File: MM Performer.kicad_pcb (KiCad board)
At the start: 4 copper layers, 75.2 x 85.7 mm, 44 parts, among them IC1 68000D, J1 VCC, J2 GND, J3 FPU Clock, U1 MC68030RC, U2 MC68881FN-SOC, U3 ATF16V8BJ, U4 ATF16V8BJ, U5 ATF16V8BJ, U6 ATF16V8BJ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

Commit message: Further signal tweaks
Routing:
- net /CLK_30: track 115.9 -> 127.8 mm
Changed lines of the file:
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@@
+	)
+	(segment
+		(start 75.507 129.725)
+		(end 75.057 130.175)
+		(width 0.4)
+		(layer "F.Cu")
+		(net 82)
 	)
 	(segment
@@
 	(segment
 		(start 70.231 130.175)
-		(end 106.68 130.175)
+		(end 75.057 130.175)
+		(width 0.4)
+		(layer "F.Cu")
+		(net 82)
+	)
+	(segment
+		(start 75.507 119.819)
+		(end 75.507 129.725)
 		(width 0.4)
 		(layer "F.Cu")
@@
 		(width 0.4)
 		(layer "F.Cu")
+		(net 82)
+	)
+	(segment
+		(start 76.454 118.872)
+		(end 75.507 119.819)
+		(width 0.4)
+		(layer "F.Cu")
+		(net 82)
+	)
+	(segment
+		(start 75.057 130.175)
+		(end 106.68 130.175)
+		(width 0.4)
+		(layer "F.Cu")

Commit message: Further tweaks
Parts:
- moved J2 8.93 mm to (106.8, 124.3)
- moved J1 8.39 mm to (97.5, 133.9)
- moved C1 7.89 mm to (105.4, 132.1), turned to 45 degrees
- moved J3 7.73 mm to (107.8, 86.2), turned to 180 degrees
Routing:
- net /CLK_30: track 127.8 -> 117.1 mm
- net /FPUCLK: track 39.5 -> 44.9 mm
- net GND: track 728.1 -> 723.6 mm
- net VCC: track 818.1 -> 814.0 mm

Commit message: Tweak placement again
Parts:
- C10: moved to B.Cu
- moved C10 2.79 mm to (69.1, 131.3)
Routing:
- net GND: track 723.6 -> 666.0 mm
- net VCC: track 814.0 -> 758.5 mm
- net /CLK_30: track 117.1 -> 121.9 mm, vias 1 -> 2
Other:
- board size 75.2 x 85.7 mm -> 75.6 x 87.1 mm

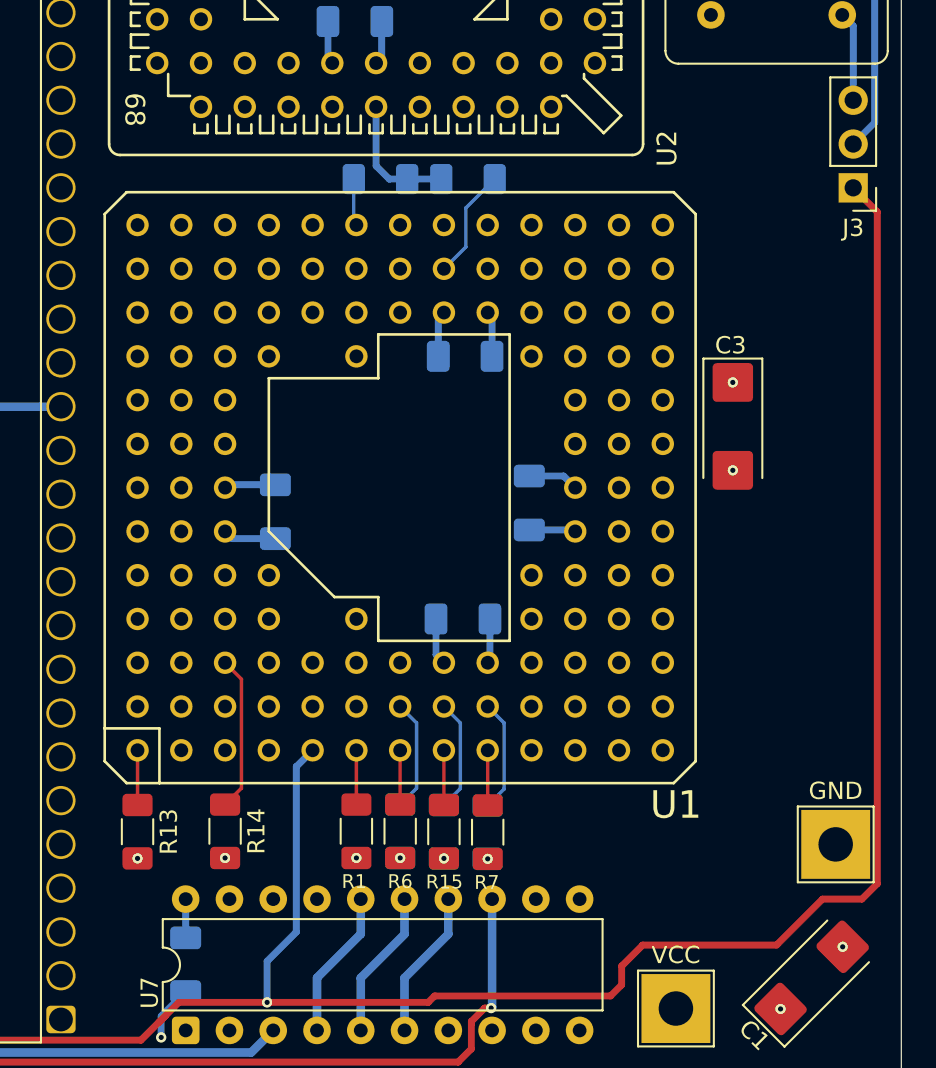
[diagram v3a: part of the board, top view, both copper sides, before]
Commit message: Reposition CPU
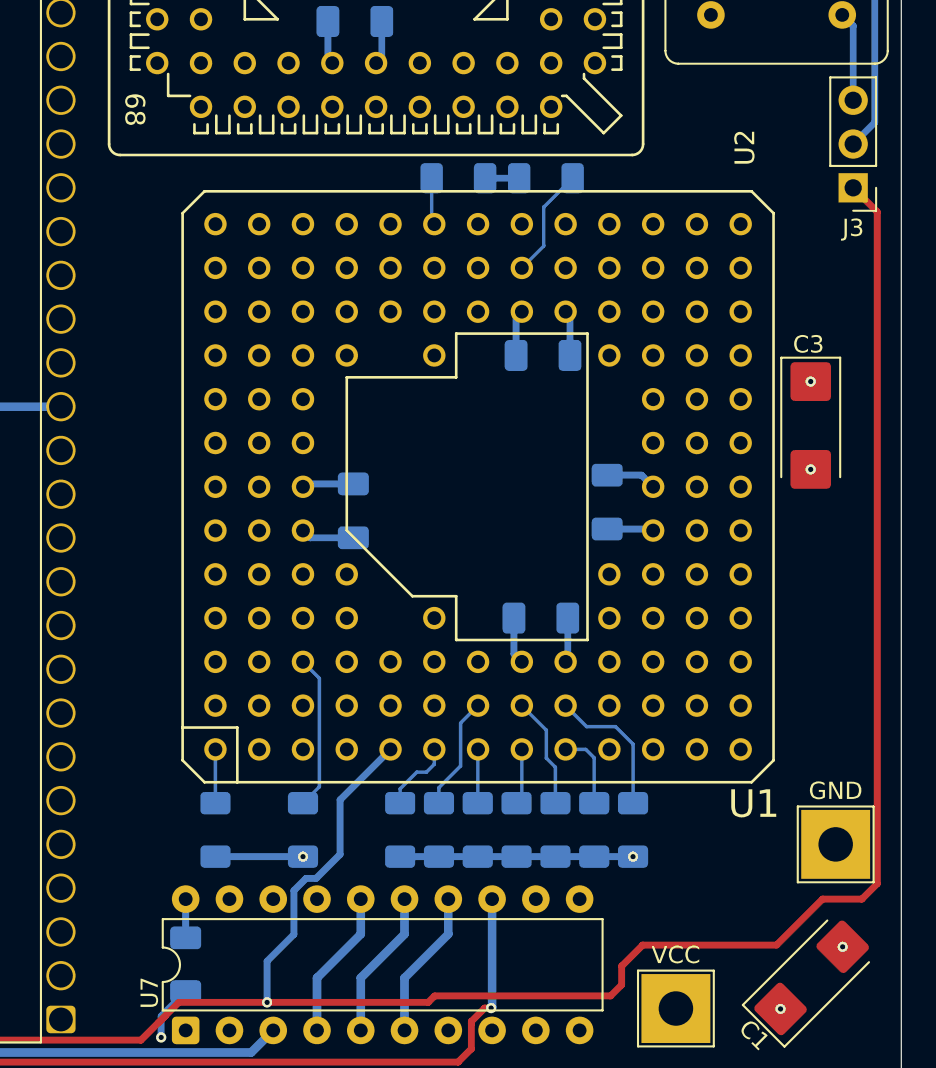
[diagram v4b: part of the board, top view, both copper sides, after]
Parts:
- R1, R13, R14, R15, R6, R7: moved to B.Cu
- moved R5 8.43 mm to (95.0, 123.5)
- moved R8 6.47 mm to (90.5, 123.5)
- moved R7 6.18 mm to (92.8, 123.5)
- moved R13 4.52 mm to (70.8, 123.5)
- moved R14 4.52 mm to (75.9, 123.5)
- moved C12 4.52 mm to (89.8, 96.0)
- moved C13 4.52 mm to (89.7, 111.2)
- moved C3 4.52 mm to (105.4, 100.0)
- moved C11 4.52 mm to (93.5, 104.5)
- moved C6 4.52 mm to (78.8, 105.0)
- moved R11 4.52 mm to (90.0, 85.7)
- moved R12 4.52 mm to (84.9, 85.7)
- moved U1 4.52 mm to (86.1, 103.6)
- moved R6 4.50 mm to (86.0, 123.5)
- moved R15 4.22 mm to (88.3, 123.5)
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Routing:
- net VCC: track 758.5 -> 749.0 mm, vias 17 -> 13
- net /CLK_30: track 121.9 -> 124.1 mm
- net //AS_30: track 6.53 -> 8.27 mm
- net //CBACK: track 3.20 -> 4.49 mm
- net //DSACK0: track 3.15 -> 4.27 mm

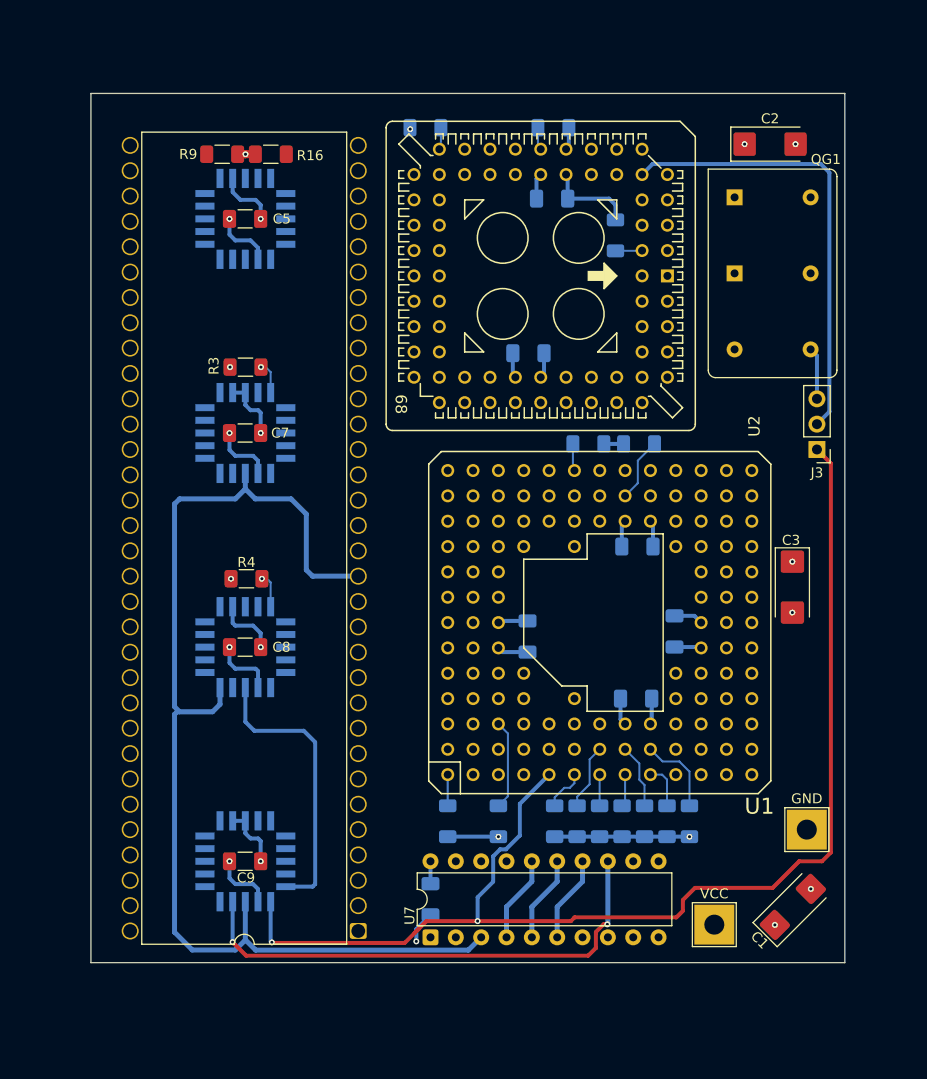
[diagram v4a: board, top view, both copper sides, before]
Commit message: Route traces, add zones
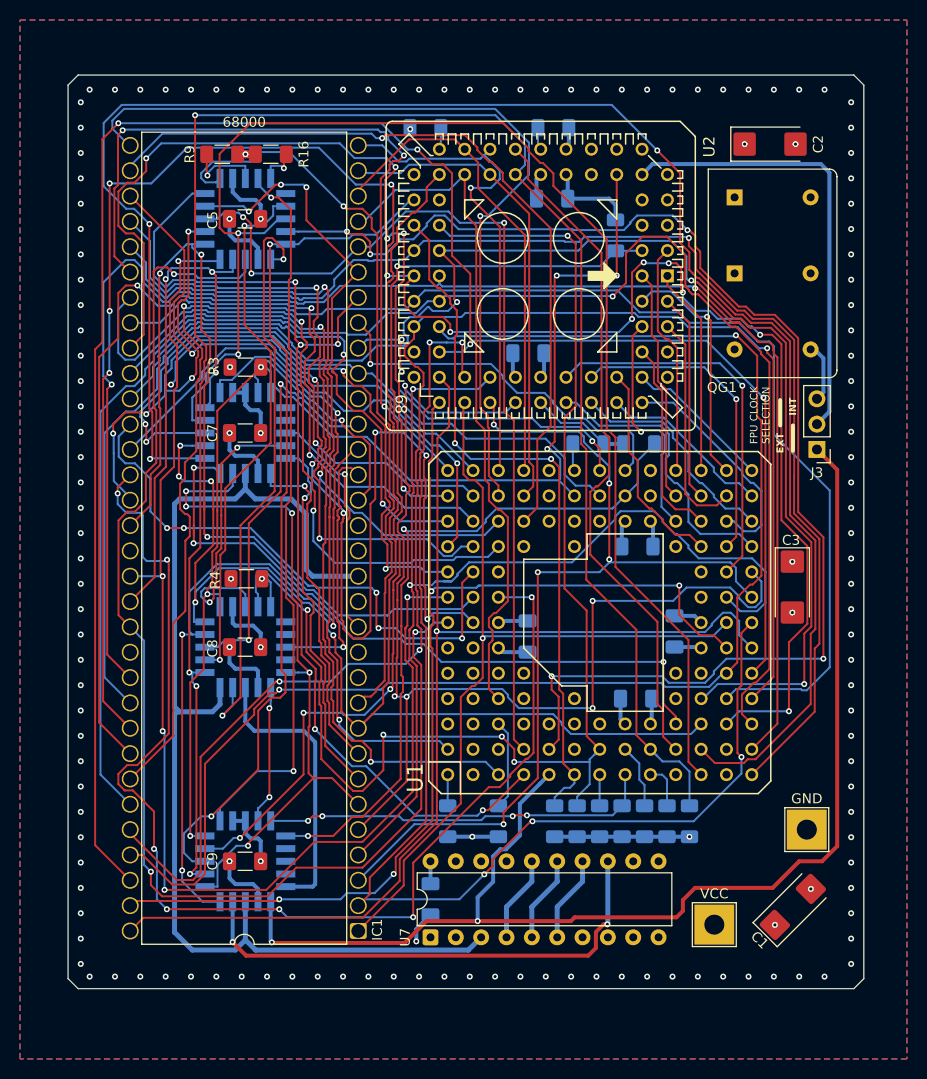
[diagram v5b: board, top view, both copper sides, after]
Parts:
- IC1: value 68000D -> 68000
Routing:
- net GND: track 665.5 -> 1001.9 mm, vias 8 -> 138
- net /D29: track 0.00 -> 199.2 mm, vias 0 -> 12
- net /D23: track 0.00 -> 195.3 mm, vias 0 -> 4
- net //AS_30: track 8.27 -> 190.7 mm, vias 0 -> 4
- net /SIZ0: track 0.00 -> 177.9 mm, vias 0 -> 3
- net /D31: track 0.00 -> 170.8 mm, vias 0 -> 2
- net /D30: track 0.00 -> 168.4 mm, vias 0 -> 3
- net /D26: track 0.00 -> 164.0 mm, vias 0 -> 1
- net /D28: track 0.00 -> 162.5 mm, vias 0 -> 2
- net /D27: track 0.00 -> 161.2 mm, vias 0 -> 1
- net /D25: track 0.00 -> 155.8 mm, vias 0 -> 3
- net /A22: track 0.00 -> 155.2 mm, vias 0 -> 10
- net //R/W: track 0.00 -> 151.6 mm, vias 0 -> 5
- net /D24: track 0.00 -> 144.0 mm, vias 0 -> 2
- net //CIIN: track 0.00 -> 140.9 mm, vias 0 -> 2
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- added copper zone on B.Cu, net GND
- added copper zone on F.Cu, net GND
- added copper zone on In2.Cu, net GND
- added copper zone on In1.Cu, net VCC
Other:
- board size 75.6 x 87.1 mm -> 79.8 x 91.6 mm
- board text added: "EXT"
- board text added: "FPU CLOCK SELECTION"
- board text added: "INT"

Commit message: Further silkscreen changes and trace rerouting
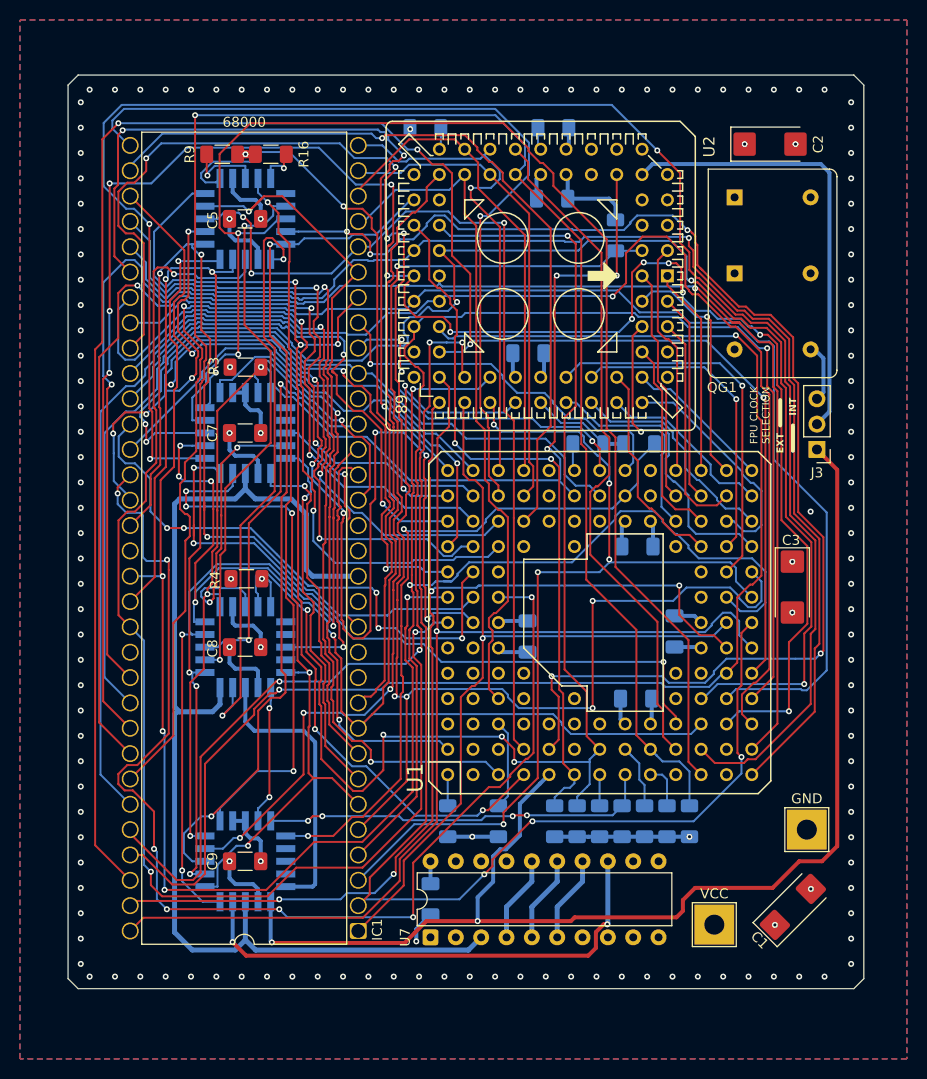
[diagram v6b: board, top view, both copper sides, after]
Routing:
- net GND: track 1001.9 -> 1006.2 mm, vias 138 -> 139
- net /FC1: track 89.8 -> 88.5 mm, vias 4 -> 2

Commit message: Begin fixing the autorouter's mess
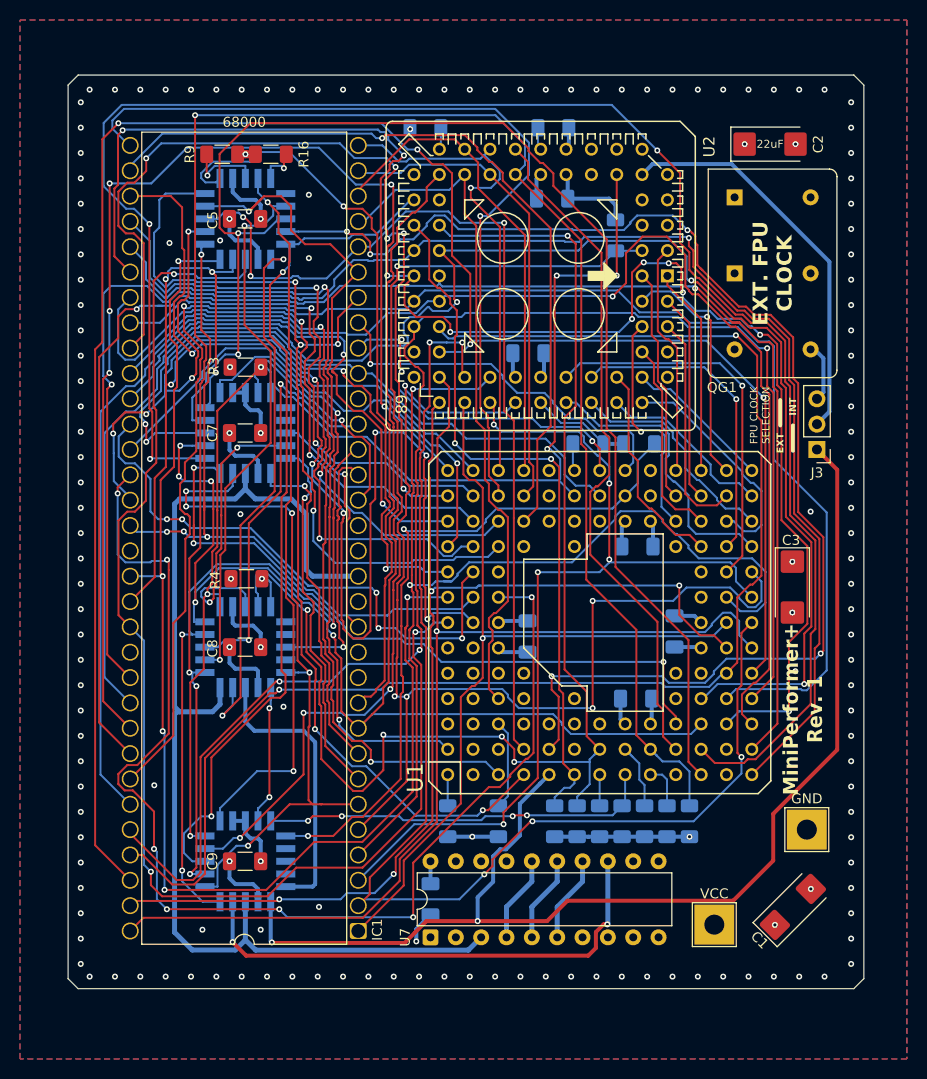
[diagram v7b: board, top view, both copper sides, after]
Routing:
- net GND: track 1006.2 -> 1051.4 mm, vias 139 -> 150
- net /A20: track 94.4 -> 70.1 mm, vias 3 -> 4
- net /FPUCLK: track 45.3 -> 40.1 mm
- net /NOFC: track 58.3 -> 54.3 mm
- net /D31: track 170.5 -> 166.9 mm
- net /CLK_30: track 125.3 -> 121.8 mm
- net /D28: track 162.5 -> 159.9 mm
- net /A7: track 53.3 -> 55.7 mm
- net /FC2: track 107.6 -> 109.2 mm
- net /FC1: track 88.5 -> 89.9 mm
- net /A23: track 129.3 -> 128.2 mm
- net /FC0: track 92.3 -> 93.1 mm
- net //AS_00: track 70.9 -> 71.5 mm
- net //FPUCS: track 86.2 -> 85.6 mm
- net /A18: track 119.8 -> 120.4 mm
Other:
- board text added: "EXT. FPU CLOCK"
- board text added: "MiniPerformer+ Rev. 1"

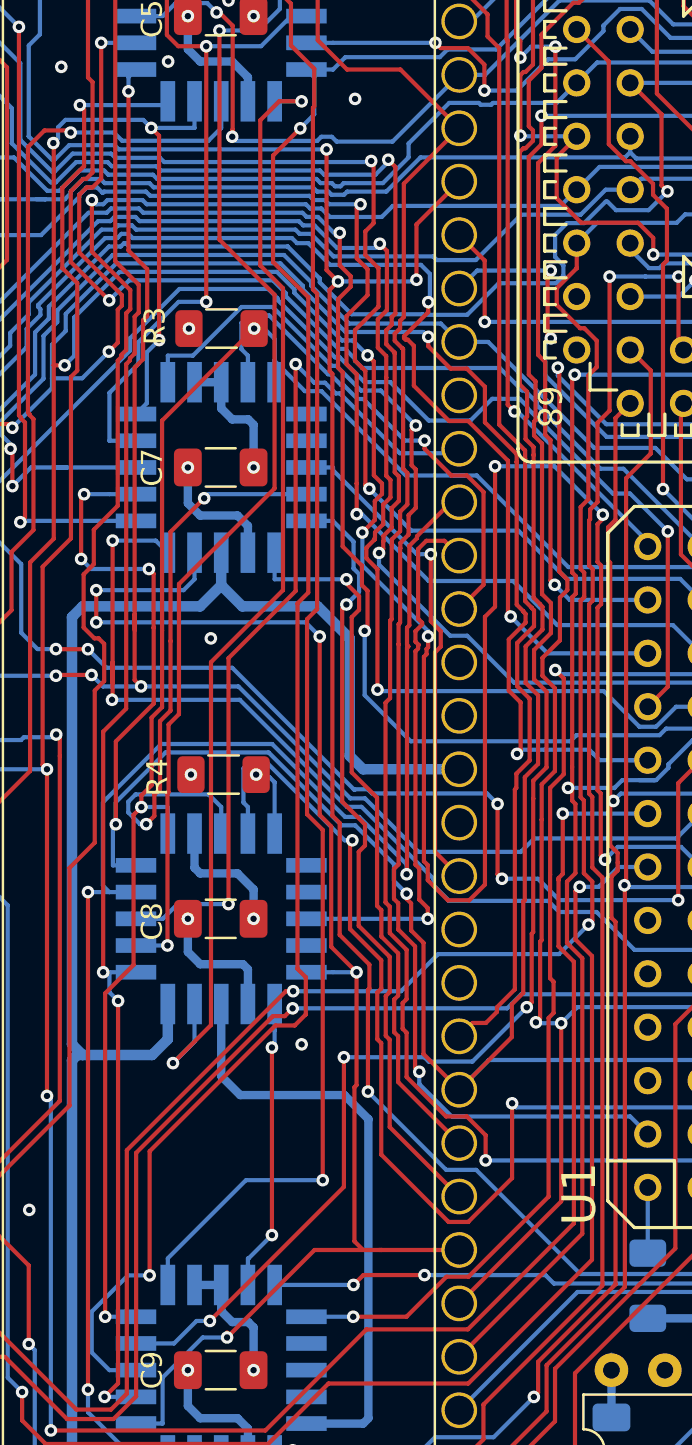
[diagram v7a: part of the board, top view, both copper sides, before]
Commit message: Further tweaks to routing
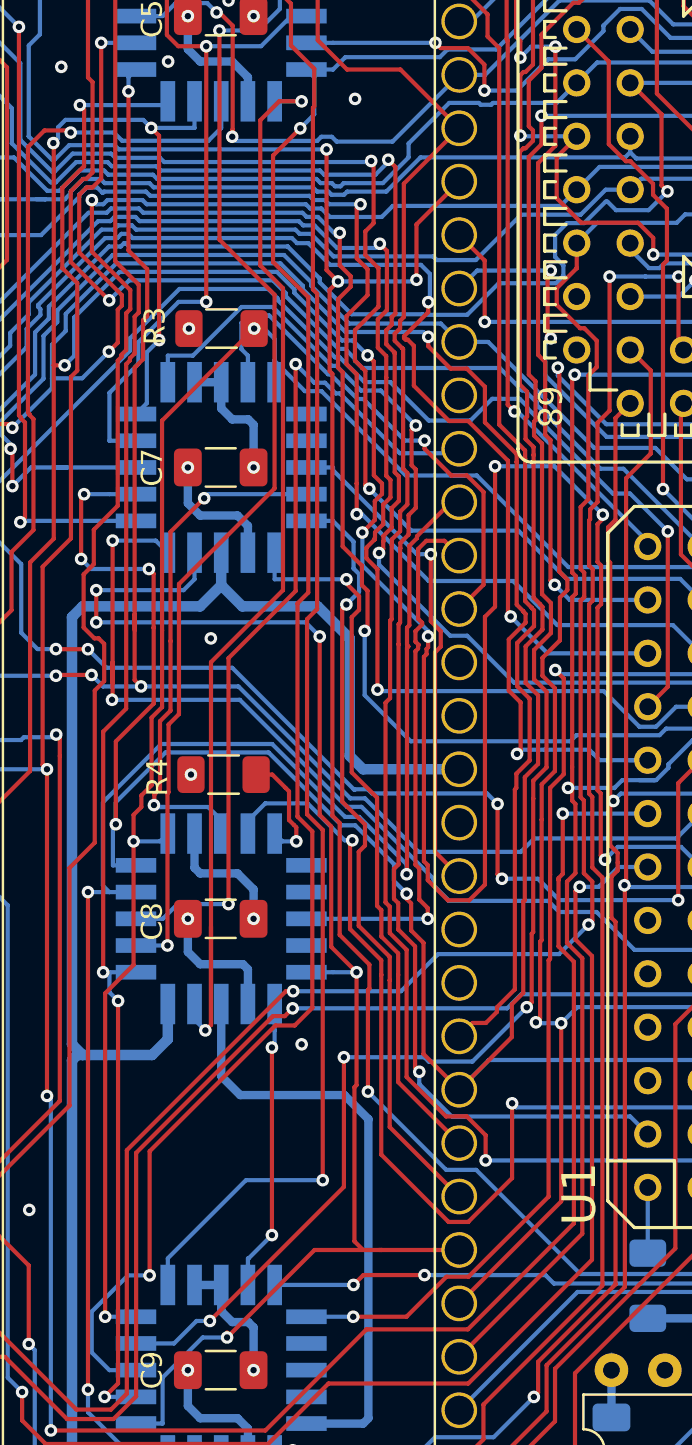
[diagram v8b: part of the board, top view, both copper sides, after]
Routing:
- net /N$7: track 29.3 -> 25.3 mm
- net //DSACK1: track 134.7 -> 131.1 mm
- net /P2.A17: track 3.47 -> 5.60 mm
- net //RESET_30: track 130.1 -> 129.4 mm
- net /NOFC: track 54.3 -> 55.0 mm
